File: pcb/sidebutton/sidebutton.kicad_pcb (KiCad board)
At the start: 2 copper layers, 19 x 33 mm, 6 parts, among them J1 Conn_01x04, SW1 SW_DIP_x01, U1 JT8P-3.2T-B10K-1-16Y

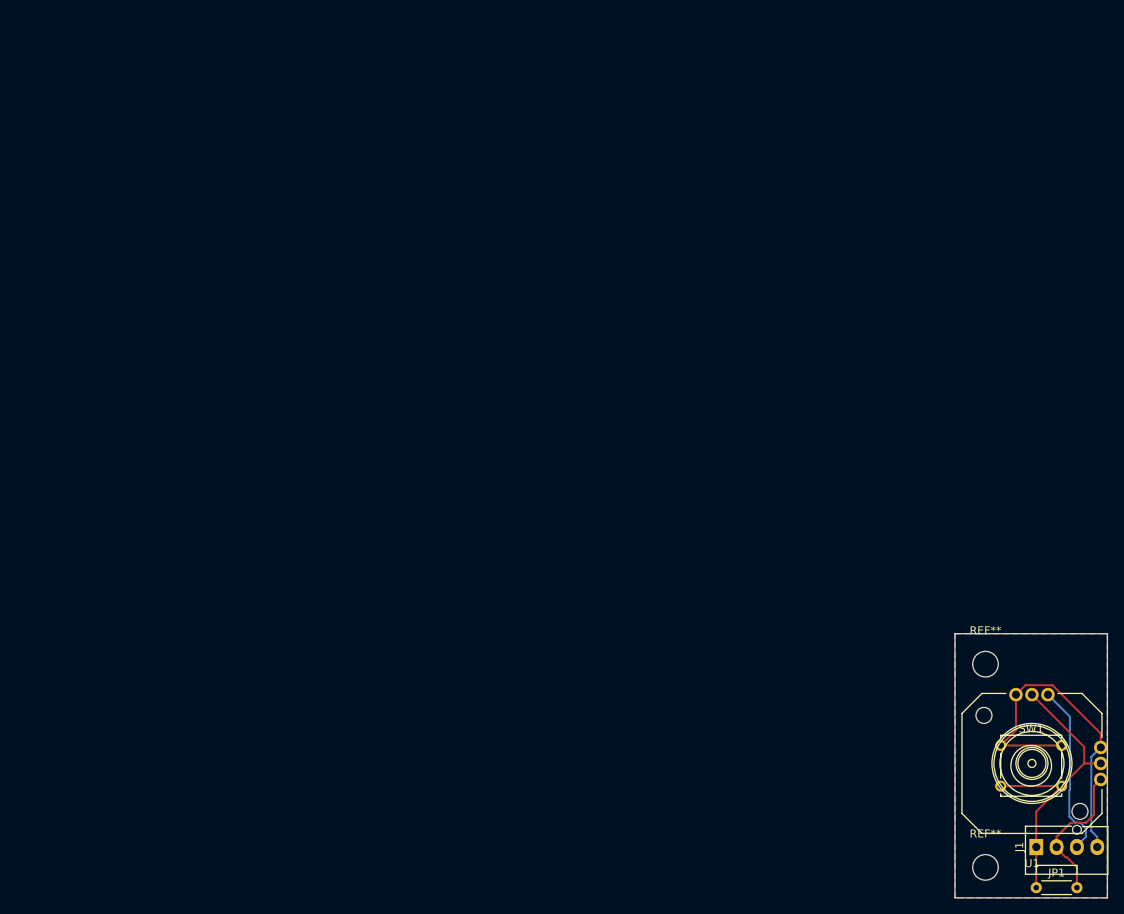
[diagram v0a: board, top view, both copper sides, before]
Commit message: fix sidebutton めっちゃブリッジしそうで怖い
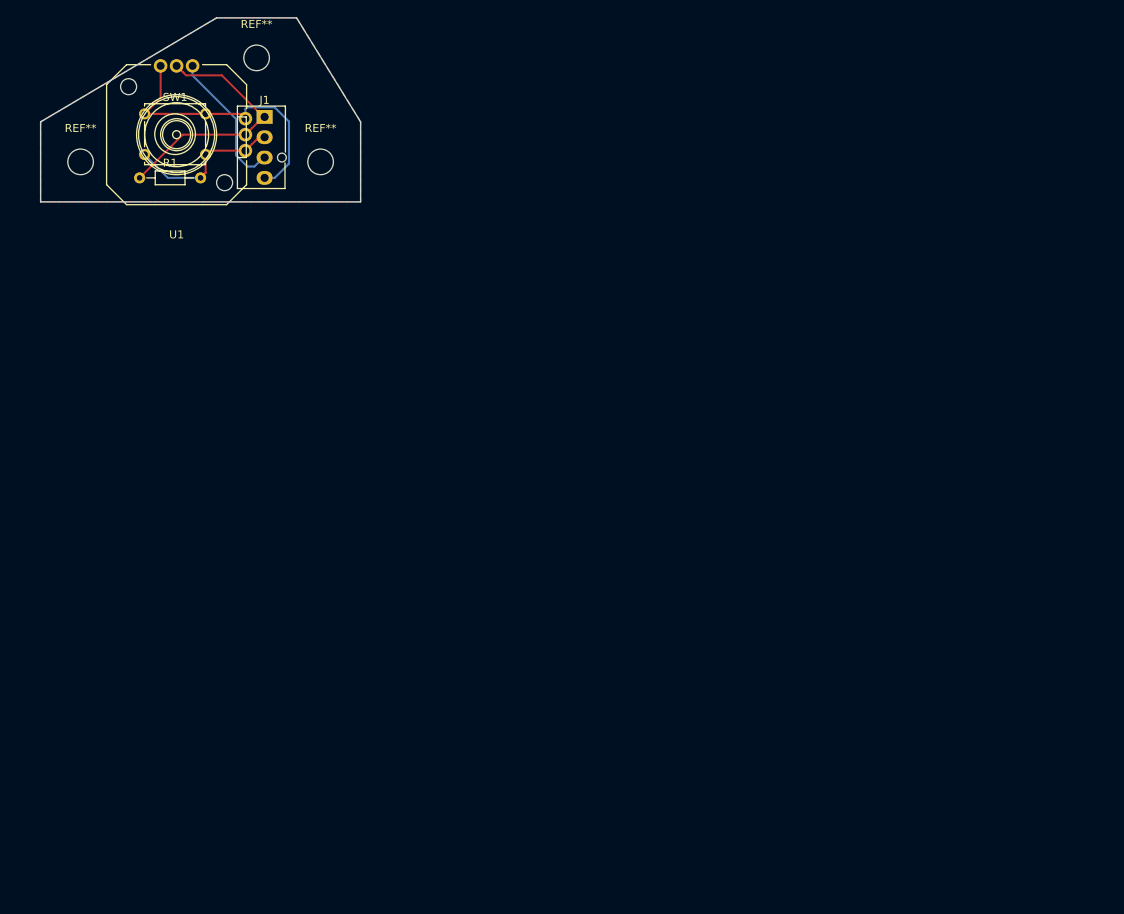
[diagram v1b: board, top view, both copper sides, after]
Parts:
- removed JP1: Jumper, Resistors_THT:R_Axial_DIN0204_L3.6mm_D1.6mm_P5.08mm_Horizontal
- removed the REF** at (118.1, 83.2)
- removed the REF** at (118.1, 57.8)
- added R1: R, Resistors_THT:R_Axial_DIN0204_L3.6mm_D1.6mm_P7.62mm_Horizontal, F.Cu at (12.4, -3.00)
- added REF**: MountingHole_3.2mm_M3, Mounting_Holes:MountingHole_3.2mm_M3, F.Cu at (5.00, -5.00)
- added REF**: MountingHole_3.2mm_M3, Mounting_Holes:MountingHole_3.2mm_M3, F.Cu at (35.0, -5.00)
- added REF**: MountingHole_3.2mm_M3, Mounting_Holes:MountingHole_3.2mm_M3, F.Cu at (27.0, -18.0)
- moved SW1 133.0 mm to (13.0, -11.0)
- moved J1 132.8 mm to (28.0, -10.6), turned to 0 degrees
- moved U1 132.7 mm to (17.0, -8.40)
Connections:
- SW1 pad 2: +5V -> /out1
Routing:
- net GND: track 43.3 -> 36.2 mm
- net +5V: track 39.0 -> 32.4 mm
- net /out2: track 21.9 -> 18.0 mm
- net /out1: track 18.1 -> 19.7 mm
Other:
- board size 19 x 33 mm -> 40 x 23 mm

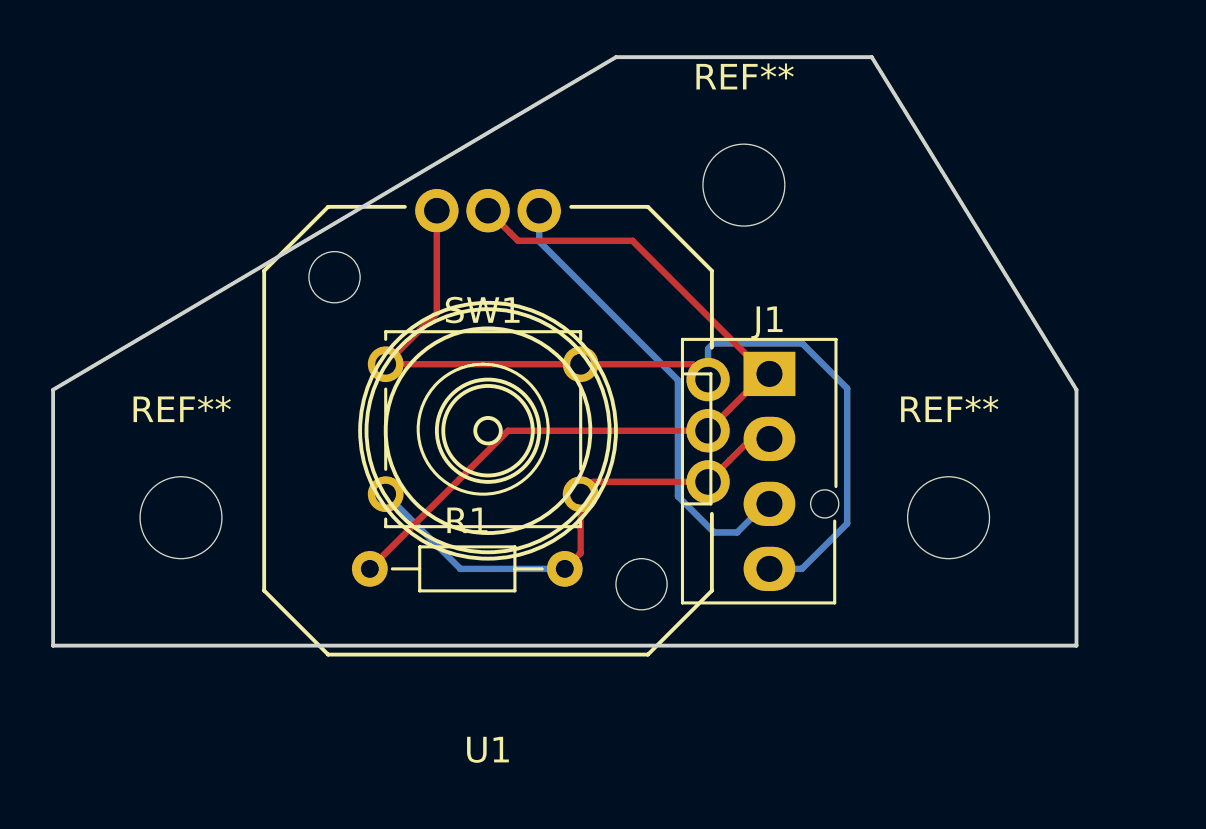
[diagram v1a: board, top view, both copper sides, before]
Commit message: sidebutton pcb became reversible
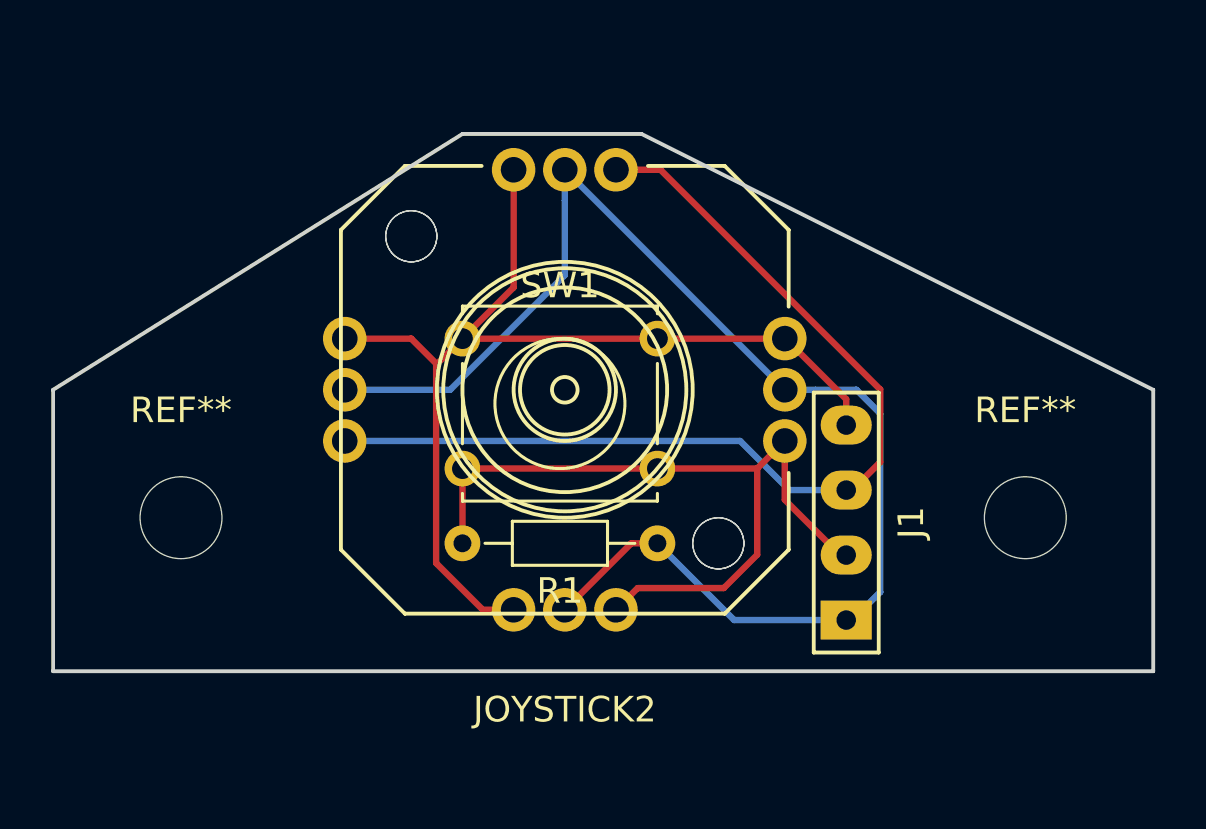
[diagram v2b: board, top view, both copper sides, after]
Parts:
- removed the REF** at (35.0, -5.00)
- removed the REF** at (27.0, -18.0)
- removed U1: JT8P-3.2T-B10K-1-16Y, 4x6t2:JT8P-3.2T-B10K-1-16Y
- added JOYSTICK1: JT8P-3.2T-B10K-1-16Y, 4x6t2:JT8P-3.2T-B10K-1-16Y, B.Cu at (20.0, -10.0)
- added JOYSTICK2: JT8P-3.2T-B10K-1-16Y, 4x6t2:JT8P-3.2T-B10K-1-16Y, F.Cu at (20.0, -10.0)
- added REF**: MountingHole_3.2mm_M3, Mounting_Holes:MountingHole_3.2mm_M3, F.Cu at (38.0, -5.00)
- J1: footprint Connectors:Fan_Pin_Header_Straight_1x04 -> 4x6t2:Wirepad_01x04
- moved R1 11.3 mm to (23.6, -4.00), turned to 180 degrees
- moved J1 6.54 mm to (31.0, -4.81), turned to 180 degrees
- moved SW1 3.16 mm to (16.0, -12.0)
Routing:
- net /out2: track 18.0 -> 38.9 mm
- net +5V: track 32.4 -> 52.9 mm
- net /out1: track 19.7 -> 31.3 mm
- net GND: track 36.2 -> 41.4 mm
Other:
- board size 40 x 23 mm -> 43 x 21 mm

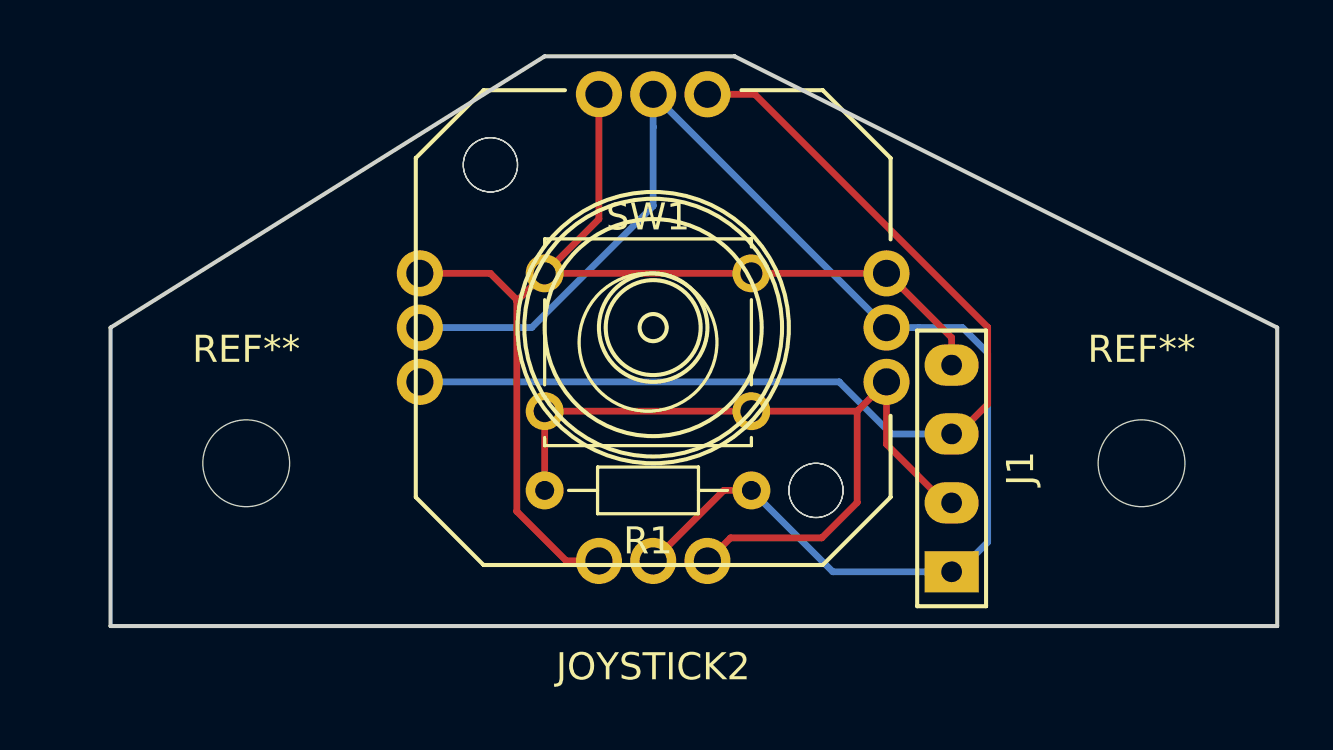
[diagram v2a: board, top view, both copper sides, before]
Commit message: fix sidebutton pcb 穴間の修正
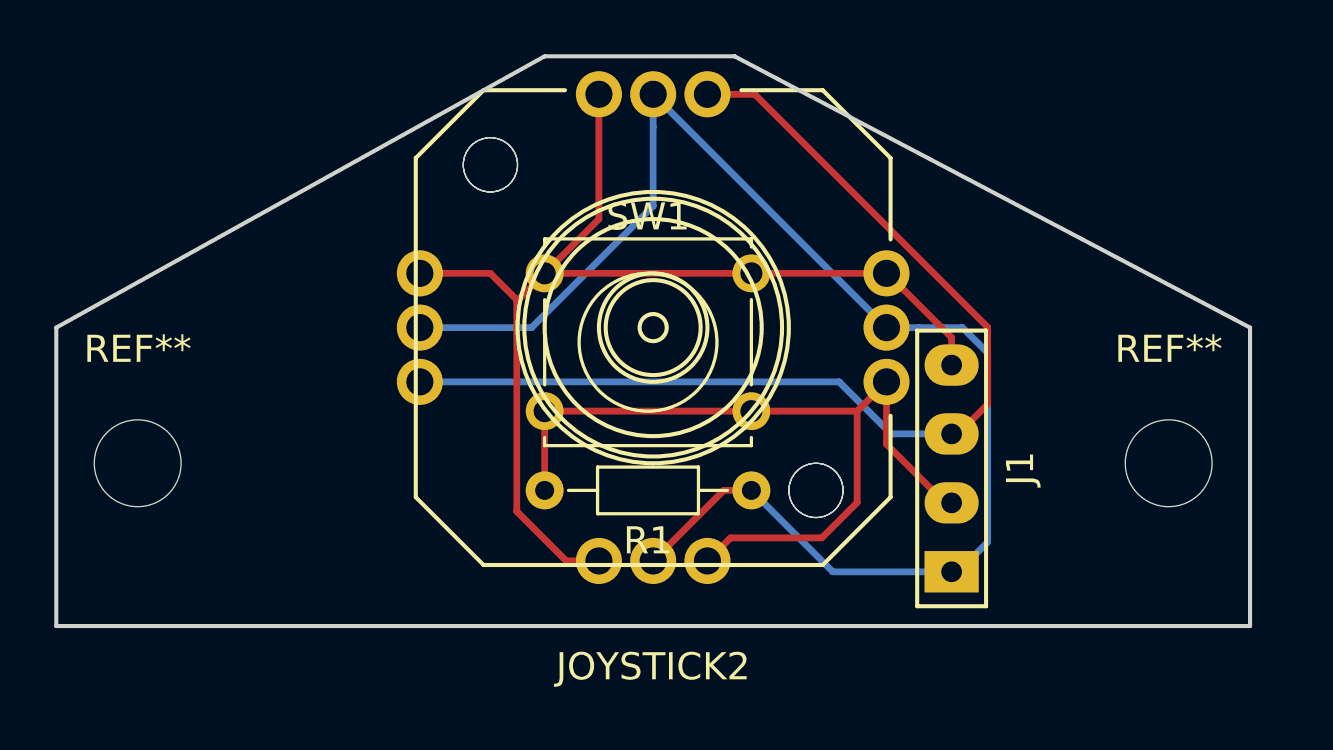
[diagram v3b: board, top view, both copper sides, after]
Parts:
- moved REF** 4.00 mm to (1.00, -5.00)
- moved REF** 1.00 mm to (39.0, -5.00)
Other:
- board size 43 x 21 mm -> 44 x 21 mm
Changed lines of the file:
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@@
     (links 18)
     (no_connects 0)
-    (area -4.560143 -20.075001 47.560143 3.578)
+    (area -2.075001 -20.075001 42.075001 1.075001)
     (thickness 1.6)
     (drawings 6)
@@
     (mod_text_size 1 1)
     (mod_text_width 0.15)
-    (pad_size 1.524 1.524)
-    (pad_drill 0.762)
+    (pad_size 3.2 3.2)
+    (pad_drill 3.2)
     (pad_to_mask_clearance 0.2)
     (aux_axis_origin 0 0)
@@
   )
   (module Mounting_Holes:MountingHole_3.2mm_M3 (layer F.Cu)
-    (at 5 -5)
+    (at 1 -5)
     (descr "Mounting Hole 3.2mm, no annular, M3")
     (tags "mounting hole 3.2mm no annular m3")
@@
   )
   (module Mounting_Holes:MountingHole_3.2mm_M3 (layer F.Cu)
-    (at 38 -5)
+    (at 39 -5)
     (descr "Mounting Hole 3.2mm, no annular, M3")
     (tags "mounting hole 3.2mm no annular m3")
@@
     (pad 1 np_thru_hole circle (at 0 0) (size 3.2 3.2) (drill 3.2) (layers *.Cu *.Mask))
   )
-  (gr_line (start 23 -20) (end 43 -10) (layer Edge.Cuts) (width 0.15))
+  (gr_line (start 23 -20) (end 42 -10) (layer Edge.Cuts) (width 0.15))
   (gr_line (start 16 -20) (end 23 -20) (layer Edge.Cuts) (width 0.15))
-  (gr_line (start 0 -10) (end 16 -20) (layer Edge.Cuts) (width 0.15))
-  (gr_line (start 0 -10) (end 0 1) (layer Edge.Cuts) (width 0.15))
-  (gr_line (start 43 -10) (end 43 1) (layer Edge.Cuts) (width 0.15))
-  (gr_line (start 0 1) (end 43 1) (layer Edge.Cuts) (width 0.15))
+  (gr_line (start -2 -10) (end 16 -20) (layer Edge.Cuts) (width 0.15))
+  (gr_line (start -2 -10) (end -2 1) (layer Edge.Cuts) (width 0.15))
+  (gr_line (start 42 -10) (end 42 1) (layer Edge.Cuts) (width 0.15))
+  (gr_line (start -2 1) (end 42 1) (layer Edge.Cuts) (width 0.15))
   (segment (start 31 -1) (end 31.238 -1) (width 0.25) (layer B.Cu) (net 1))
   (segment (start 32.32801 -2.09001) (end 32.32801 -9.071496) (width 0.25) (layer B.Cu) (net 1))
@@
     (polygon
       (pts
-        (xy 16 -20) (xy 23 -20) (xy 43 -10) (xy 43 1) (xy 0 1)
-        (xy 0 -10)
+        (xy 16 -20) (xy 23 -20) (xy 42 -10) (xy 42 1) (xy -2 1)
+        (xy -2 -10)
       )
     )
@@
     (polygon
       (pts
-        (xy 0 -10) (xy 0 1) (xy 43 1) (xy 43 -10) (xy 23 -20)
+        (xy -2 -10) (xy -2 1) (xy 42 1) (xy 42 -10) (xy 23 -20)
         (xy 16 -20)
       )

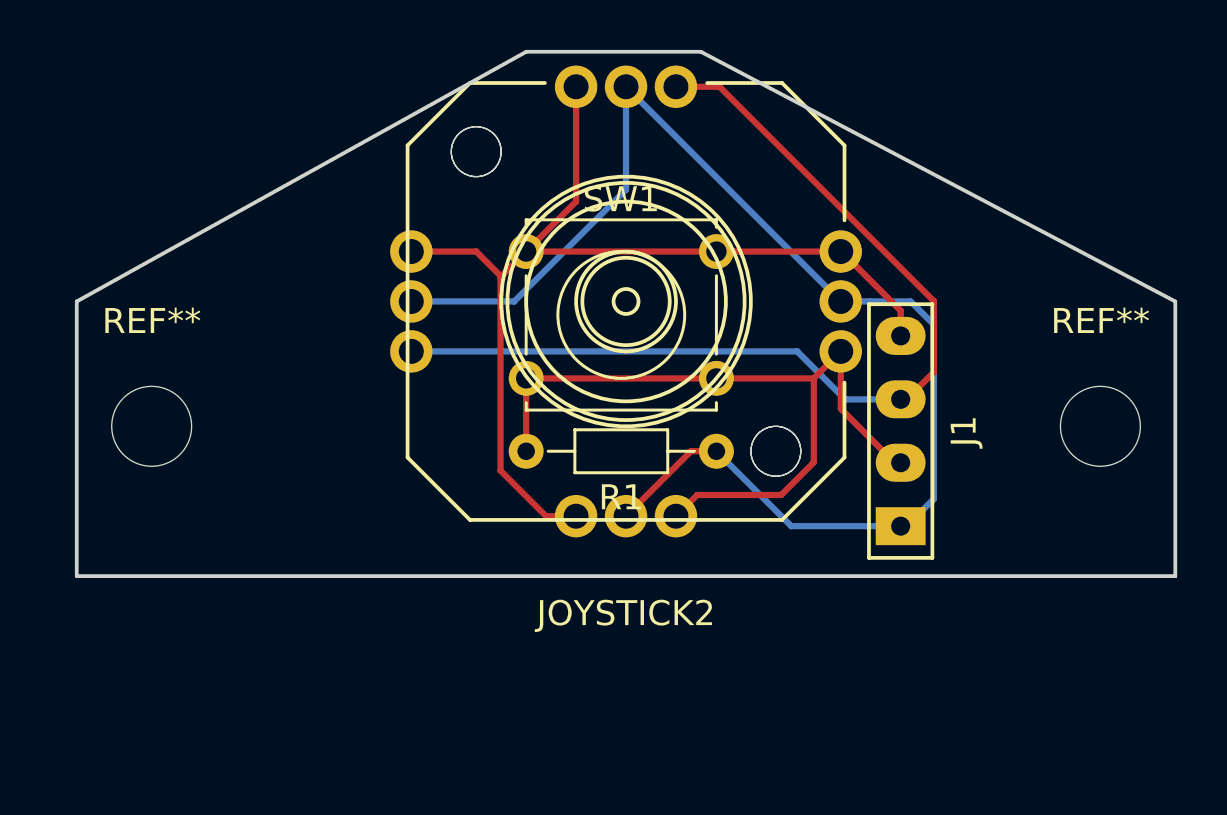
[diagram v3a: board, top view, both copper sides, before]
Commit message: fix sidebutton pcb design
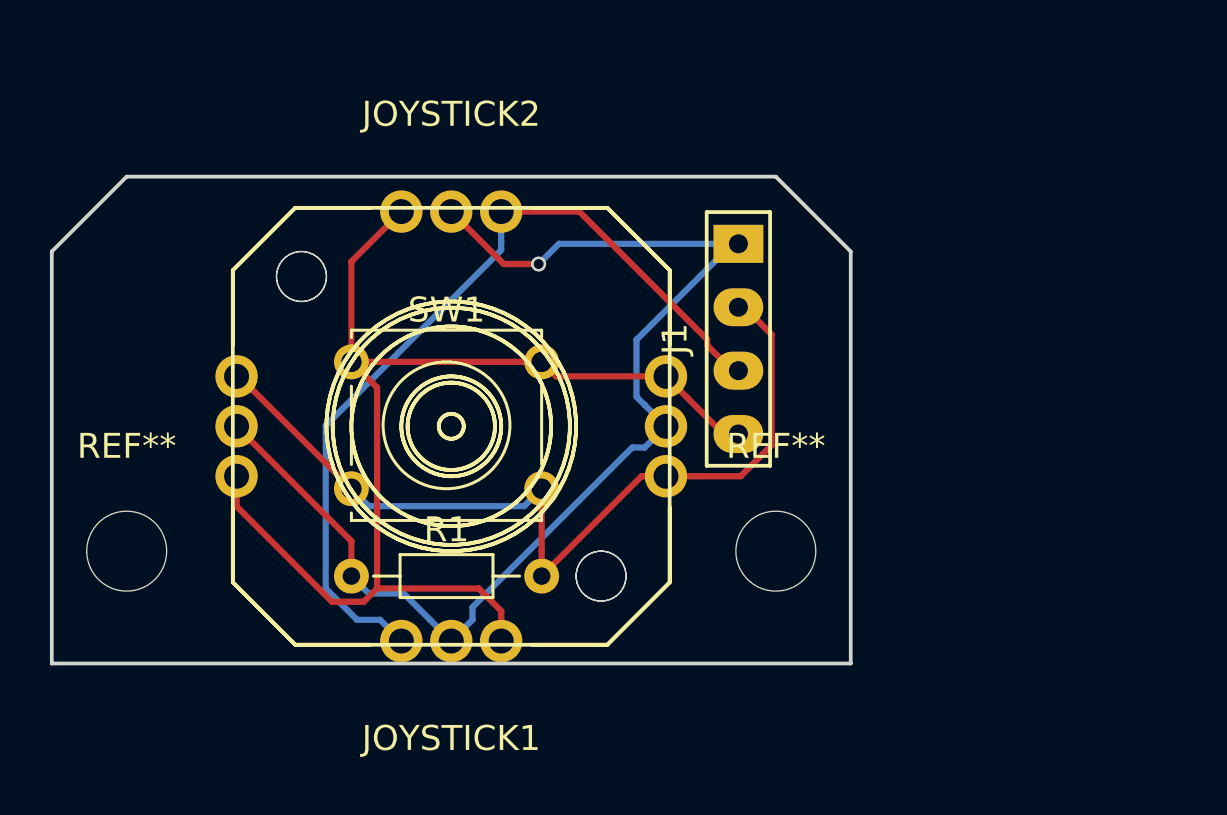
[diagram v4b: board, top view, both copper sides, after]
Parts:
- removed the REF** at (1.00, -5.00)
- removed the REF** at (39.0, -5.00)
- added REF**: MountingHole_3.2mm_M3, Mounting_Holes:MountingHole_3.2mm_M3, F.Cu at (0.00, 0.00)
- added REF**: MountingHole_3.2mm_M3, Mounting_Holes:MountingHole_3.2mm_M3, F.Cu at (26.0, 0.00)
- JOYSTICK1: moved to F.Cu
- moved R1 15.5 mm to (9.00, 1.00), turned to 0 degrees
- moved JOYSTICK1 8.60 mm to (13.0, -5.00), turned to 0 degrees
- moved JOYSTICK2 8.60 mm to (13.0, -5.00), turned to 180 degrees
- moved SW1 8.28 mm to (9.00, -7.58)
- moved J1 7.47 mm to (24.5, -8.50), turned to 0 degrees
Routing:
- net GND: track 41.4 -> 48.2 mm
- net +5V: track 52.9 -> 47.8 mm, vias 0 -> 1
- net /out2: track 38.9 -> 34.2 mm
- net /out1: track 31.3 -> 35.8 mm
- removed copper zone on B.Cu, net GND
- removed copper zone on F.Cu, net GND
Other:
- board size 44 x 21 mm -> 32 x 19.5 mm
